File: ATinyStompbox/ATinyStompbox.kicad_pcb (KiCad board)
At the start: 2 copper layers, 33.3 x 120 mm, 55 parts, among them J1 CONN_01X05, J10 6.5mm_JACK_TRS_6PINS, J11 CONN_01X04, J12 Con_JackIN, J13 Con_JackOUT, J14 CONN_01X04, J15 Con_DC, J16 Con_BAT, J17 StompDrillHole, J18 Con_3-5V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

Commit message: new netlist
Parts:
- added J20: BoardDimension, 8BitMixtape_Stomp:CaseDim, F.Cu at (101.3, 58.7)
- J21: footprint 8BitMixtape_Stomp:DimensionGuides -> 8BitMixtape_Stomp:StompCase_Full
- moved J21 110.6 mm to (164.3, 35.8)

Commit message: small improvements
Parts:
- removed CV1: POT 10K lin, 8BitMixtapes_all:Mixtape_Pot_Alps_RK09K_Horizontal
- removed Main1: POT 10K lin Sleeve, 8BitMixtape_Stomp:Mixtape_Pot_Alps_RK09L_Sleve_Single_Horizontal
- removed Vol1: POT 10k, 8BitMixtapes_all:Mixtape_Pot_Alps_RK09K_Horizontal
- added POT1-CV1: POT 10K lin, 8BitMixtapes_all:Mixtape_Pot_Alps_RK09K_Horizontal, F.Cu at (85.2, 58.5)
- added POT2-Main1: POT 10K lin Sleeve, 8BitMixtape_Stomp:Mixtape_Pot_Alps_RK09L_Sleve_Single_Horizontal, F.Cu at (74.7, 84.0)
- added POT3-Vol1: POT 10k, 8BitMixtapes_all:Mixtape_Pot_Alps_RK09K_Horizontal, F.Cu at (64.1, 58.7)
- D1: footprint LEDs:LED_D5.0mm -> LEDs:LED_PLCC_2835_Handsoldering
- D2: value LED -> LED_Dual_AAC; footprint LEDs:LED_D5.0mm_FlatTop -> 8BitMixtape_Stomp:Stomp_LED-Ring_DUAL
- moved D2 17.3 mm to (69.6, 140.0)
- moved D1 1.49 mm to (72.4, 40.4)
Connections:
- D2 pad 1: Net-(D2-Pad1) -> VCC
- J16 pad 2: +BATT -> DC_in
- J9 pad 3: +BATT -> (no net)
- SW5 pad 5: Net-(D2-Pad1) -> Net-(D2-Pad3)

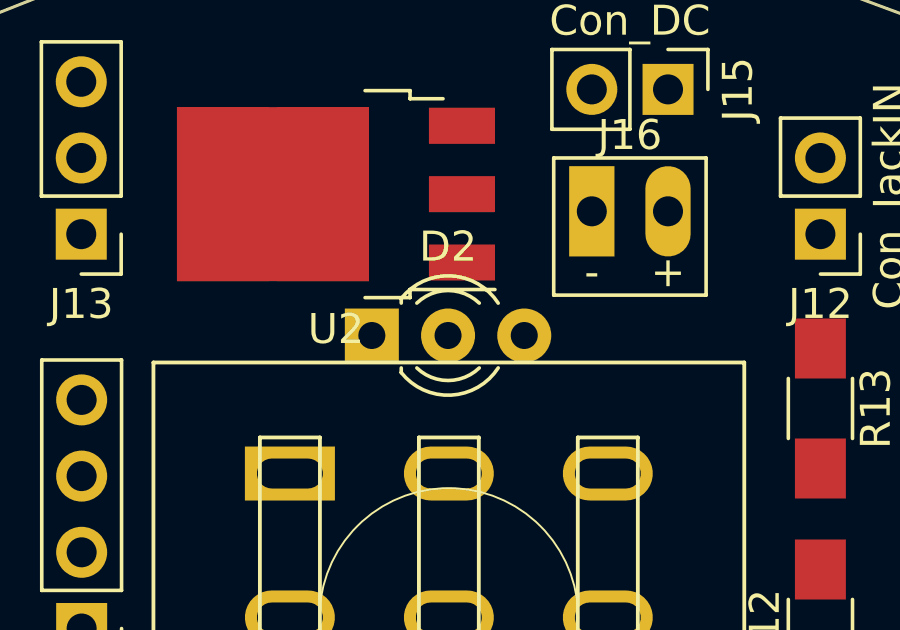
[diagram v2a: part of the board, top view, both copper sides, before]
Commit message: new schematics for DualLED
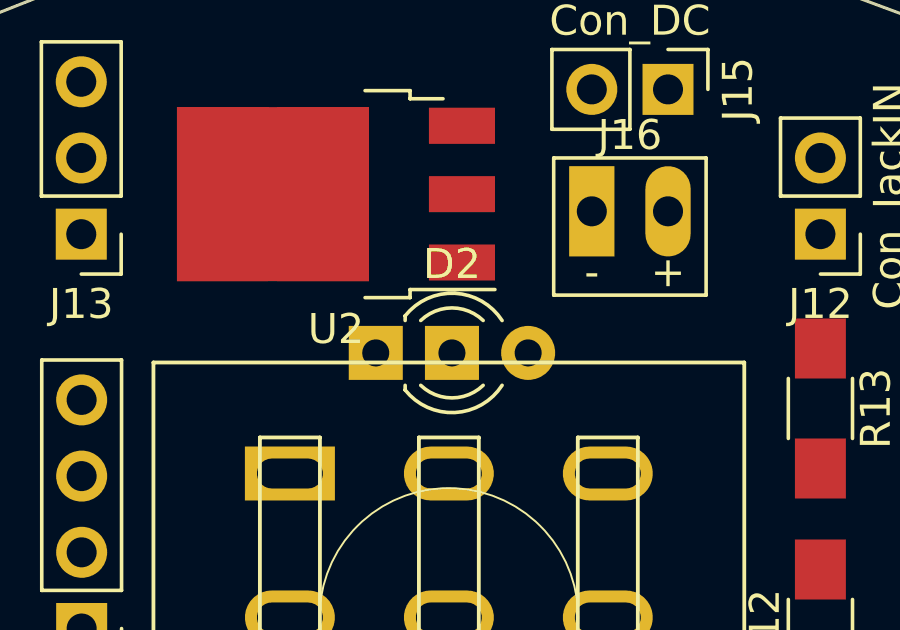
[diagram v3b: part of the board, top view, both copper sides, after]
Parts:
- D2: value LED_Dual_AAC -> LED_Dual_CCA
- moved D2 0.59 mm to (69.8, 140.6)
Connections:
- D2 pad 1: VCC -> PB1
- D2 pad 2: VCC -> Net-(D2-Pad2)
- D2 pad 3: Net-(D2-Pad3) -> VCC
- SW5 pad 5: Net-(D2-Pad3) -> Net-(D2-Pad2)
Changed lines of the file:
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@@
 (kicad_pcb (version 4) (host pcbnew 4.0.7-e0-6372~58~ubuntu16.04.1)
   (general
-    (links 0)
+    (links 100)
     (no_connects 100)
     (area 55.48041 38.651023 88.897544 158.750543)
@@
   (net 29 +3V3)
   (net 30 "Net-(D3-Pad4)")
-  (net 31 "Net-(D2-Pad3)")
-  (net 32 "Net-(POT1-CV1-Pad2)")
-  (net 33 "Net-(POT2-Main1-Pad2)")
-  (net 34 "Net-(POT2-Main1-Pad1)")
+  (net 31 "Net-(POT1-CV1-Pad2)")
+  (net 32 "Net-(POT2-Main1-Pad2)")
+  (net 33 "Net-(POT2-Main1-Pad1)")
+  (net 34 "Net-(D2-Pad2)")
   (net_class Default "This is the default net class."
     (clearance 0.3)
@@
     (add_net "Net-(D-OUT1-Pad2)")
     (add_net "Net-(D1-Pad1)")
-    (add_net "Net-(D2-Pad3)")
+    (add_net "Net-(D2-Pad2)")
     (add_net "Net-(D3-Pad4)")
     (add_net "Net-(J5-Pad1)")
@@
       (net 1 VCC))
     (pad 2 smd rect (at 2 0 270) (size 2 1.7) (layers B.Cu B.Paste B.Mask)
-      (net 34 "Net-(POT2-Main1-Pad1)"))
+      (net 33 "Net-(POT2-Main1-Pad1)"))
     (model ${KISYS3DMOD}/Resistors_SMD.3dshapes/R_1206.wrl
       (at (xyz 0 0 0))
@@
       (net 21 PB2/A1))
     (pad 2 smd rect (at 2 0 90) (size 2 1.7) (layers B.Cu B.Paste B.Mask)
-      (net 32 "Net-(POT1-CV1-Pad2)"))
+      (net 31 "Net-(POT1-CV1-Pad2)"))
     (model ${KISYS3DMOD}/Resistors_SMD.3dshapes/R_1206.wrl
       (at (xyz 0 0 0))
@@
       (net 20 PB4/A2))
     (pad 2 smd rect (at 2 0 270) (size 2 1.7) (layers B.Cu B.Paste B.Mask)
-      (net 33 "Net-(POT2-Main1-Pad2)"))
+      (net 32 "Net-(POT2-Main1-Pad2)"))
     (model ${KISYS3DMOD}/Resistors_SMD.3dshapes/R_1206.wrl
       (at (xyz 0 0 0))
@@
       (net 13 "Net-(R13-Pad1)"))
     (pad 5 thru_hole oval (at 0 0 90) (size 1.8 3) (drill oval 1 2.2) (layers *.Cu *.Mask)
-      (net 31 "Net-(D2-Pad3)"))
+      (net 34 "Net-(D2-Pad2)"))
     (pad 6 thru_hole oval (at 0 4.79806 90) (size 1.8 3) (drill oval 1 2.2) (layers *.Cu *.Mask)
       (net 12 "Net-(R12-Pad1)"))
@@
       (net 2 GND))
     (pad 2 thru_hole circle (at 0 -2.5 90) (size 1.8 1.8) (drill 1) (layers *.Cu *.Mask)
-      (net 32 "Net-(POT1-CV1-Pad2)"))
+      (net 31 "Net-(POT1-CV1-Pad2)"))
     (pad 1 thru_hole circle (at 0 0 90) (size 1.8 1.8) (drill 1) (layers *.Cu *.Mask)
       (net 15 Sound_IN))
@@
       (net 2 GND))
     (pad 2 thru_hole circle (at 0 -2.5 90) (size 1.8 1.8) (drill 1) (layers *.Cu *.Mask)
-      (net 33 "Net-(POT2-Main1-Pad2)"))
+      (net 32 "Net-(POT2-Main1-Pad2)"))
     (pad 1 thru_hole circle (at 0 0 90) (size 1.8 1.8) (drill 1) (layers *.Cu *.Mask)
-      (net 34 "Net-(POT2-Main1-Pad1)"))
+      (net 33 "Net-(POT2-Main1-Pad1)"))
     (pad "" np_thru_hole oval (at 7.5 -7.25 90) (size 4 2) (drill oval 3 1) (layers *.Cu *.Mask))
     (pad "" np_thru_hole oval (at 7.5 2.25 90) (size 4 2) (drill oval 3 1) (layers *.Cu *.Mask))
@@
   )
   (module 8BitMixtape_Stomp:Stomp_LED-Ring_DUAL (layer F.Cu)
-    (at 69.63 140.03)
+    (at 69.76 140.61)
     (descr "LED, diameter 3.0mm, 2 pins, diameter 3.0mm, 3 pins, http://www.kingbright.com/attachments/file/psearch/000/00/00/L-3VSURKCGKC(Ver.8A).pdf")
     (tags "LED diameter 3.0mm 2 pins diameter 3.0mm 3 pins")
@@
       (effects (font (size 1 1) (thickness 0.15)))
     )
-    (fp_text value LED_Dual_AAC (at 2.54 2.96) (layer F.Fab)
+    (fp_text value LED_Dual_CCA (at 2.54 2.96) (layer F.Fab)
       (effects (font (size 1 1) (thickness 0.15)))
     )
@@
     (fp_line (start 6.25 2.25) (end 6.25 -2.25) (layer F.CrtYd) (width 0.05))
     (fp_line (start 6.25 -2.25) (end -1.15 -2.25) (layer F.CrtYd) (width 0.05))
-    (pad 3 thru_hole rect (at 0 0) (size 1.8 1.8) (drill 0.9) (layers *.Cu *.Mask)
-      (net 31 "Net-(D2-Pad3)"))
-    (pad 2 thru_hole circle (at 2.54 0) (size 1.8 1.8) (drill 0.9) (layers *.Cu *.Mask)
-      (net 1 VCC))
-    (pad 1 thru_hole circle (at 5.08 0) (size 1.8 1.8) (drill 0.9) (layers *.Cu *.Mask)
+    (pad 1 thru_hole rect (at 0 0) (size 1.8 1.8) (drill 0.9) (layers *.Cu *.Mask)
+      (net 22 PB1))
+    (pad 2 thru_hole rect (at 2.54 0) (size 1.8 1.8) (drill 0.9) (layers *.Cu *.Mask)
+      (net 34 "Net-(D2-Pad2)"))
+    (pad 3 thru_hole circle (at 5.08 0) (size 1.8 1.8) (drill 0.9) (layers *.Cu *.Mask)
       (net 1 VCC))
     (model ${KISYS3DMOD}/LEDs.3dshapes/LED_D3.0mm-3.wrl
